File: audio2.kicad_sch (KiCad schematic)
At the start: 10 parts, among them J10 AudioJack3_SwitchTR, J7 AudioJack3_SwitchTR, U3 LM4950TS

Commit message: save state
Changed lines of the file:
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@@
 	)
 	(hierarchical_label "CODEC{WS BCLK DOUT DIN MCLK}"
-		(shape bidirectional)
+		(shape input)
 		(at 69.85 158.75 180)
 		(effects

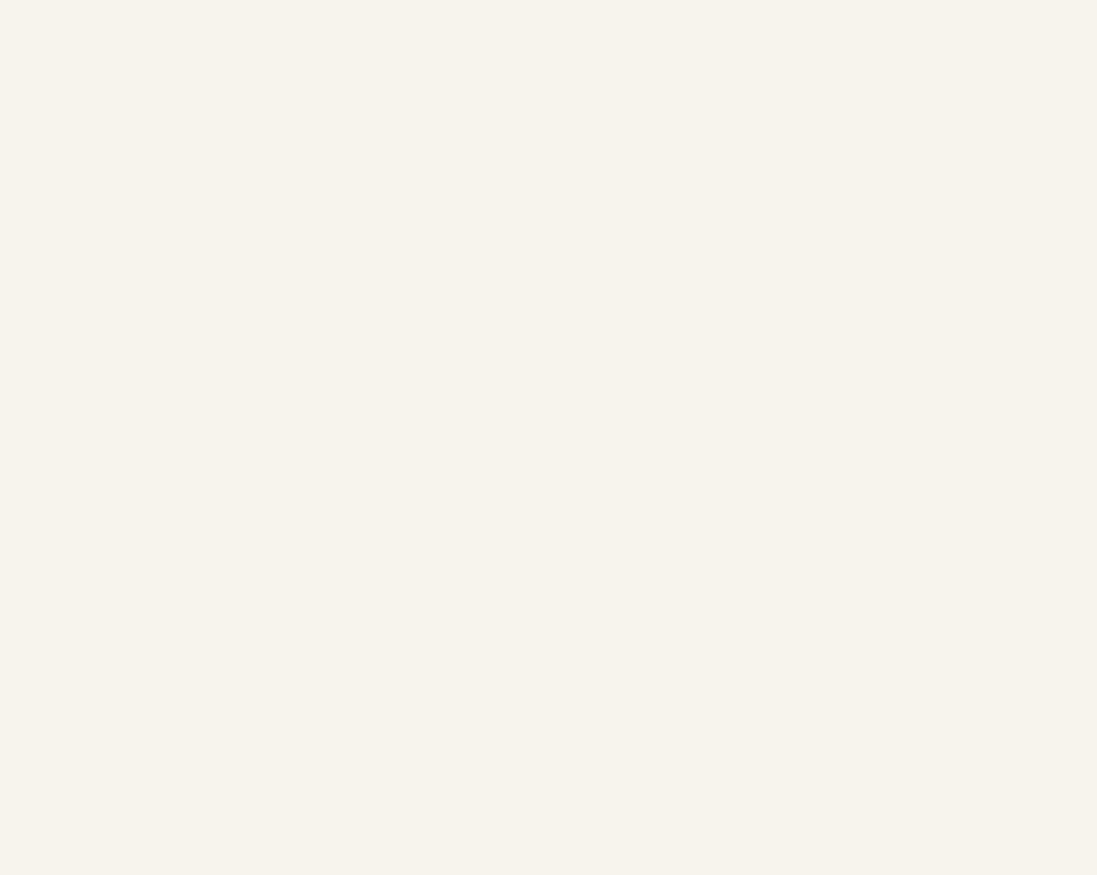
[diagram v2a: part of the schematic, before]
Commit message: Add ES9822QPRO
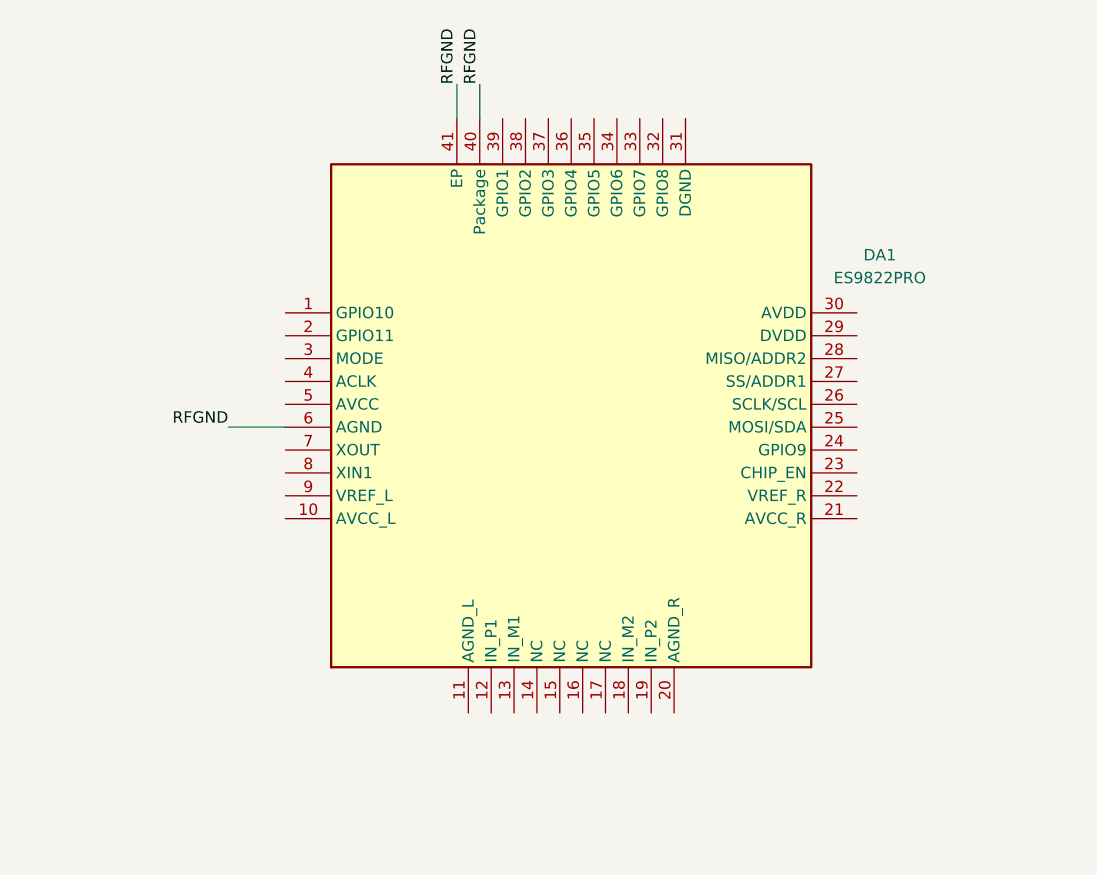
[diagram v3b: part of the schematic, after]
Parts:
- added DA1: ES9822PRO, Package_DFN_QFN:QFN-40-1EP_6x6mm_P0.5mm_EP4.6x4.6mm_ThermalVias, symbol hftrx_lib:ES9822PRO
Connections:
- net RFGND: now also DA1.40 (Package), DA1.41 (EP), DA1.6 (AGND)
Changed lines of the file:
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@@
+	(wire
+		(pts
+			(xy 168.91 59.69) (xy 175.26 59.69)
+		)
+		(stroke
+			(width 0)
+			(type default)
+		)
+	)
 	(wire
 		(pts
@@
 	(wire
 		(pts
+			(xy 196.85 21.59) (xy 196.85 25.4)
+		)
+		(stroke
+			(width 0)
+			(type default)
+		)
+	)
+	(wire
+		(pts
 			(xy 100.33 147.32) (xy 106.68 147.32)
 		)
@@
 		(pts
 			(xy 313.69 130.81) (xy 354.33 130.81)
+		)
+		(stroke
+			(width 0)
+			(type default)
+		)
+	)
+	(wire
+		(pts
+			(xy 194.31 21.59) (xy 194.31 25.4)
 		)
 		(stroke
@@
 		)
 	)
+	(label "RFGND"
+		(at 194.31 21.59 90)
+		(effects
+			(font
+				(size 1.27 1.27)
+			)
+			(justify left bottom)
+		)
+	)
 	(label "SPI.SCLK"
 		(at 114.3 208.28 0)
@@
 		)
 	)
+	(label "RFGND"
+		(at 196.85 21.59 90)
+		(effects
+			(font
+				(size 1.27 1.27)
+			)
+			(justify left bottom)
+		)
+	)
 	(label "CODEC1_RHP"
 		(at 303.53 114.3 180)
@@
 			)
 			(justify left bottom)
+		)
+	)
+	(label "RFGND"
+		(at 168.91 59.69 180)
+		(effects
+			(font
+				(size 1.27 1.27)
+			)
+			(justify right bottom)
 		)
 	)
@@
 					(unit 1)
 				)
+			)
+		)
+	)
+	(symbol
+		(lib_id "hftrx_lib:ES9822PRO")
+		(at 207.01 58.42 0)
+		(unit 1)
+		(body_style 1)
+		(exclude_from_sim no)
+		(in_bom yes)
+		(on_board yes)
+		(in_pos_files yes)
+		(dnp no)
+		(fields_autoplaced yes)
+		(property "Reference" "DA1"
+			(at 241.3 40.5698 0)
+			(show_name no)
+			(do_not_autoplace no)
+			(effects
+				(font
+					(size 1.27 1.27)
+				)
+			)
+		)
+		(property "Value" "ES9822PRO"
+			(at 241.3 43.1098 0)
+			(show_name no)
+			(do_not_autoplace no)
+			(effects
+				(font
+					(size 1.27 1.27)
+				)
+			)
+		)
+		(property "Footprint" "Package_DFN_QFN:QFN-40-1EP_6x6mm_P0.5mm_EP4.6x4.6mm_ThermalVias"
+			(at 180.34 29.845 0)
+			(hide yes)
+			(show_name no)
+			(do_not_autoplace no)
+			(effects
+				(font
+					(size 1.27 1.27)
+				)
+				(justify right)
+			)
+		)
+		(property "Datasheet" ""
+			(at 180.34 29.845 0)
+			(hide yes)
+			(show_name no)
+			(do_not_autoplace no)
+			(effects
+				(font
+					(size 1.27 1.27)
+				)
+				(justify right)
+			)
+		)
+		(property "Description" ""
+			(at 180.34 29.845 0)
+			(hide yes)
+			(show_name no)
+			(do_not_autoplace no)
+			(effects
+				(font
+					(size 1.27 1.27)
+				)
+				(justify left)
+			)
+		)
+		(pin "13"
+		)
+		(pin "25"
+		)
+		(pin "22"
+		)
+		(pin "32"
+		)
+		(pin "14"
+		)
+		(pin "35"
+		)
+		(pin "36"
+		)
+		(pin "18"
+		)
+		(pin "21"
+		)
+		(pin "38"
+		)
+		(pin "28"
+		)
+		(pin "20"
+		)
+		(pin "37"
+		)
+		(pin "39"
+		)
+		(pin "34"
+		)
+		(pin "31"
+		)
+		(pin "40"
+		)
+		(pin "12"
+		)
+		(pin "15"
+		)
+		(pin "16"
+		)
+		(pin "17"
+		)
+		(pin "19"
+		)
+		(pin "23"
+		)
+		(pin "24"
+		)
+		(pin "27"
+		)
+		(pin "26"
+		)
+		(pin "29"
+		)
+		(pin "30"
+		)
+		(pin "33"
+		)
+		(pin "41"
+		)
+		(pin "10"
+		)
+		(pin "11"
+		)
+		(pin "6"
+		)
+		(pin "1"
+		)
+		(pin "3"
+		)
+		(pin "2"
+		)
+		(pin "4"
+		)
+		(pin "5"
+		)
+		(pin "7"
+		)
+		(pin "8"
+		)
+		(pin "9"
+		)
+		(instances
+			(project "testprj"
+				(path "/423c1216-1c87-4878-aa19-5de0f026118b/7d000037-c70c-4768-ba53-1b13c87ff30e"
+					(reference "DA1")
+					(unit 1)
+				)

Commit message: Использование power symbols
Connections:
- net RFGND: now also U3.8 (BYP)
